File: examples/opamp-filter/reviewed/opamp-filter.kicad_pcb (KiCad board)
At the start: 2 copper layers, 58 x 42 mm, 22 parts, among them J1 IN, J2 5V, J3 OUT, U1 MCP6001R, U2 MCP6001R

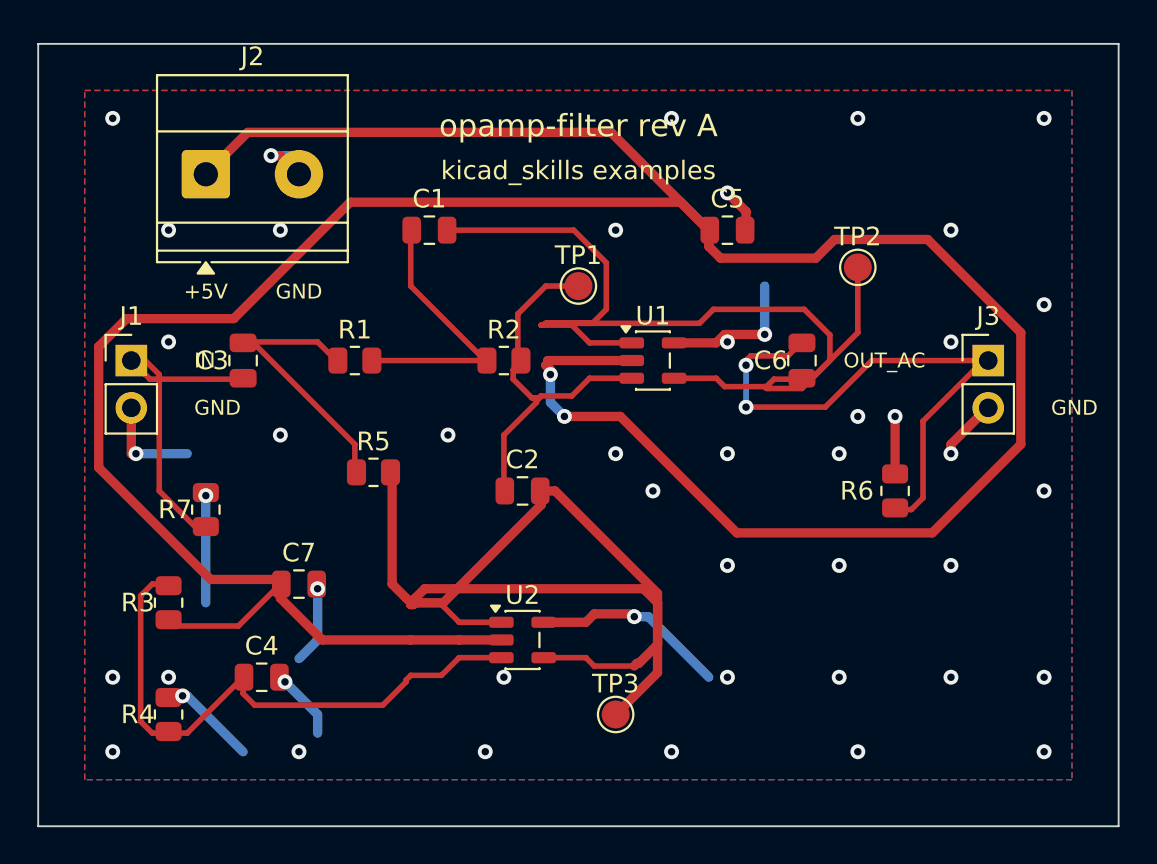
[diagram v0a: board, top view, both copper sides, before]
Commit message: Measure the copper that goes out and comes back, and the text drawn on text
The reviewer sent screenshots with circles on them. Two kinds: strings
printed through each other on the schematics, and copper that leaves a
pad, travels three sides of a rectangle and arrives four millimetres
away. Neither had a rule that could see it - `text_over_wire` measured
text against nets and nothing measured text against text, and
`route.detour` weighs a whole net, which averages one bad connection
away under any ratio worth setting.

New rule `route.wander`: one continuous run of copper - pad or junction
at each end - against the shortest way between those two ends that
clears the packages in between. The baseline walks the perimeter of
whatever the straight line crosses, so an opamp's feedback wrap is
measured against going round the package rather than through it. On
KiCad's 18 demo boards it fires once at the shipped 2.0x.

`readability.text_over_text` and `_over_wire` are regraded info: they
fire on 14 and 10 of those 18 human sheets. That is the estimate
talking, not the drawing. `ai-generated` still promotes both to errors,
so every generated design has to have none - and the five examples do.

What the two rules then made us fix:

* a net label's anchor cannot move, but its reading direction can. Each
  name is now offered the four quarters of its anchor and takes the
  first that prints over nothing. Power symbol names and PWR_FLAG names
  get the same treatment - four grounds on one row printed GNGNGNGND.
  Schematic text overlaps: buck 1, motor 2, carrier 1, fpga 7, all to 0.
* a plane crossing was priced at forty times front copper per
  millimetre, which is a prohibition, not a price: one millimetre of
  crossing bought a forty millimetre tour and the boards had grown
  them. Thirty is where neither `route.wander` nor `route.return_path`
  fires. Buck, motor and carrier now have no wander findings.
* `write_variant` resolves the routes a second time, so the
  straight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
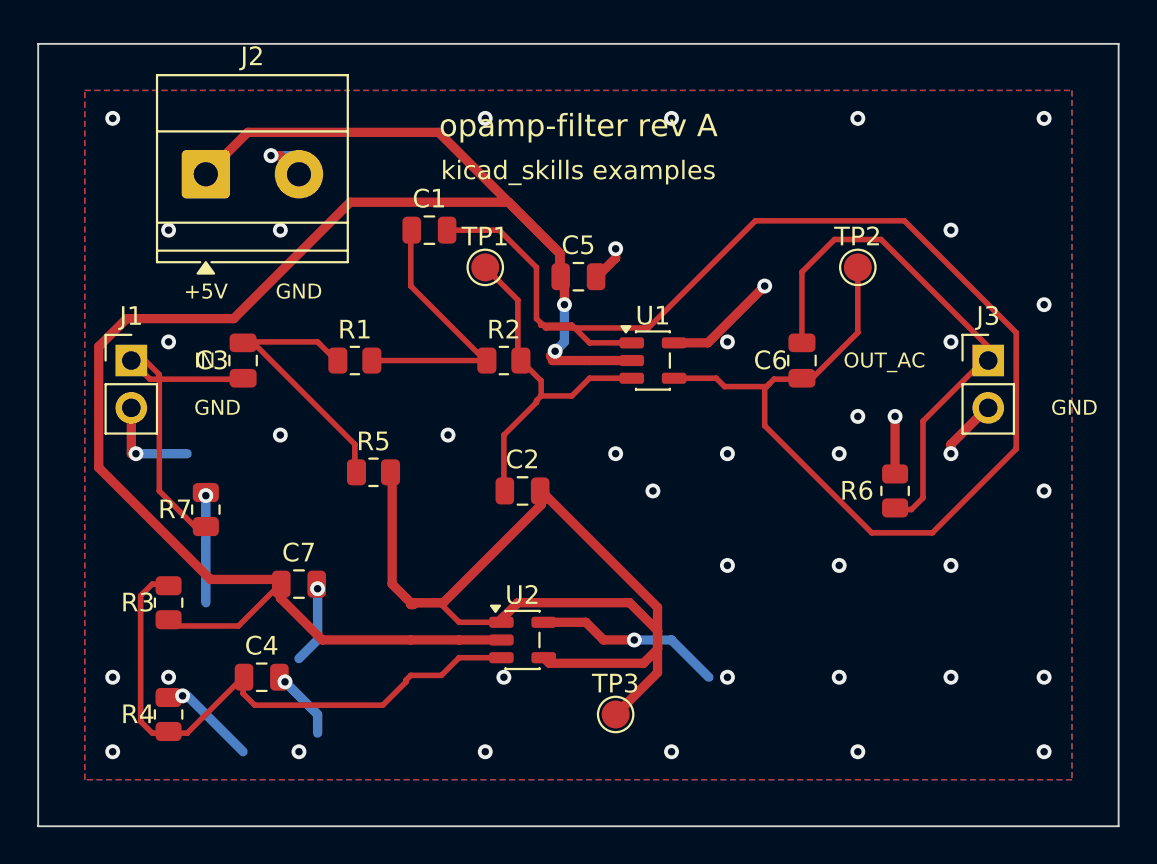
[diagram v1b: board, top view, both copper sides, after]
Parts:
- moved C5 8.38 mm to (129.0, 72.5)
- moved TP1 5.10 mm to (124.0, 72.0)
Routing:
- net +5V: track 169.8 -> 103.1 mm
- net /OUT: track 57.6 -> 85.4 mm
- net /VREF: track 61.8 -> 55.5 mm
- net GND: track 55.4 -> 53.0 mm
- net /OUT_AC: track 30.7 -> 28.4 mm, vias 2 -> 0
- net /FILT_IN: track 20.8 -> 19.3 mm

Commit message: Stop hiding the hairpins behind the pads they are drawn on
The reviewer said the 135 degree bends and the odd-angle runs were still
there. They were. `route.acute_angle` skipped any corner within a pad's
*radius*, and a 0805's radius is 0.47 mm, which covers the five or six
ordinary corners a chamfered pad entry leaves inside it. Eleven of the
thirteen hairpins on these five boards sat in that shadow, because a pad
is exactly where a route that has to double back does it.

The exemption is the pad's connection point now, not a disc around it.
Two branches leaving one pad stay exempt - the pad's own copper fills the
wedge, so it is not an acid trap - but nought degrees never is: that is
one run drawn twice, and no pad excuses it.

Then the generator had to stop making them:

* `_untraced` drops the copper a second run lays on top of the first.
  The shorter is inside the longer and carries nothing it does not; both
  get trimmed, because dropping only the duplicate leaves the other
  hanging over the gap, which is `route.stub`. It runs before the runs
  are joined, while the pair is still two tracks sharing an end - once
  joined, the shared point is usually a pad, and the clean-up passes pin
  those precisely so they cannot take copper off them.
* `_straighten` only takes the direct line when it lands on the 45 grid.
  Between two pads at whatever coordinates their packages give them it
  usually does not: last round it made a nine millimetre run at 169.7
  degrees, which is the slip-of-the-mouse angle `route.odd_angle` is for.

Measured across the five boards: off-grid segments 1 to 0, 180 degree
reversals 6 to 0, and the motor board's `route.return_path` finding went
with the 11 mm of copper it was measuring.

Three corners survive, all on the FPGA board, all where a knee lands a
fraction past where its own two legs cross - legs of 0.07 and 0.25 mm on
two, 0.15 and 0.5 mm on the third. Refusing a knee that short is worse:
the segment then keeps the angle it had, a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
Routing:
- net GND: track 53.0 -> 53.8 mm
- net /FILT_IN: track 19.3 -> 20.1 mm
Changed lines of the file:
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@@
 	(segment (start 129.6 77.95) (end 128.65 78.9) (width 0.3) (layer "F.Cu") (net 3))
 	(segment (start 128.65 78.9) (end 127.0 78.9) (width 0.3) (layer "F.Cu") (net 3))
-	(segment (start 134.1375 76.05) (end 135.95 76.05) (width 0.5) (layer "F.Cu") (net 1))
-	(segment (start 135.95 76.05) (end 139.0 73.0) (width 0.5) (layer "F.Cu") (net 1))
+	(segment (start 134.1375 76.05) (end 136.4 76.05) (width 0.5) (layer "F.Cu") (net 1))
+	(segment (start 136.4 76.05) (end 136.85 75.6) (width 0.5) (layer "F.Cu") (net 1))
+	(segment (start 136.85 75.6) (end 137.925 75.6) (width 0.5) (layer "F.Cu") (net 1))
+	(segment (start 137.925 75.6) (end 139.0 74.525) (width 0.5) (layer "F.Cu") (net 1))
+	(segment (start 139.0 74.525) (end 139.0 73.0) (width 0.5) (layer "F.Cu") (net 1))
 	(segment (start 134.1375 77.95) (end 136.4 77.95) (width 0.3) (layer "F.Cu") (net 7))
 	(segment (start 136.4 77.95) (end 136.85 78.4) (width 0.3) (layer "F.Cu") (net 7))
@@
 	(segment (start 111.0 94.875) (end 111.0 94.25) (width 0.3) (layer "F.Cu") (net 6))
 	(segment (start 111.0 94.25) (end 111.05 94.2) (width 0.3) (layer "F.Cu") (net 6))
-	(segment (start 111.05 94.2) (end 111.05 94.0) (width 0.3) (layer "F.Cu") (net 6))
-	(segment (start 111.05 94.0) (end 110.8 94.25) (width 0.3) (layer "F.Cu") (net 6))
+	(segment (start 111.05 94.2) (end 110.95 94.1) (width 0.3) (layer "F.Cu") (net 6))
+	(segment (start 110.95 94.1) (end 110.8 94.25) (width 0.3) (layer "F.Cu") (net 6))
 	(segment (start 110.8 94.25) (end 110.75 94.25) (width 0.3) (layer "F.Cu") (net 6))
 	(segment (start 110.75 94.25) (end 108.0 97.0) (width 0.3) (layer "F.Cu") (net 6))
@@
 	(segment (start 108.75 86.0) (end 108.9125 86.0) (width 0.3) (layer "F.Cu") (net 4))
 	(segment (start 108.9125 86.0) (end 109.0 85.9125) (width 0.3) (layer "F.Cu") (net 4))
-	(segment (start 116.0875 77.0) (end 115.8375 76.75) (width 0.3) (layer "F.Cu") (net 5))
-	(segment (start 115.8375 76.75) (end 115.75 76.75) (width 0.3) (layer "F.Cu") (net 5))
-	(segment (start 115.75 76.75) (end 115.0 76.0) (width 0.3) (layer "F.Cu") (net 5))
-	(segment (start 115.0 76.0) (end 111.25 76.0) (width 0.3) (layer "F.Cu") (net 5))
-	(segment (start 111.25 76.0) (end 111.2 76.05) (width 0.3) (layer "F.Cu") (net 5))
-	(segment (start 111.2 76.05) (end 111.0 76.05) (width 0.3) (layer "F.Cu") (net 5))
+	(segment (start 111.2 76.05) (end 111.25 76.0) (width 0.3) (layer "F.Cu") (net 5))
+	(segment (start 111.25 76.0) (end 115.0 76.0) (width 0.3) (layer "F.Cu") (net 5))
+	(segment (start 115.0 76.0) (end 115.75 76.75) (width 0.3) (layer "F.Cu") (net 5))
+	(segment (start 115.75 76.75) (end 115.8375 76.75) (width 0.3) (layer "F.Cu") (net 5))
+	(segment (start 115.8375 76.75) (end 116.0875 77.0) (width 0.3) (layer "F.Cu") (net 5))
 	(segment (start 111.0 76.05) (end 111.2 76.05) (width 0.3) (layer "F.Cu") (net 5))
 	(segment (start 111.2 76.05) (end 111.25 76.0) (width 0.3) (layer "F.Cu") (net 5))
@@
 	(segment (start 117.0 82.9125) (end 117.0875 83.0) (width 0.3) (layer "F.Cu") (net 5))
 	(segment (start 117.9125 77.0) (end 124.0875 77.0) (width 0.3) (layer "F.Cu") (net 10))
-	(segment (start 124.0875 77.0) (end 124.0 77.0) (width 0.3) (layer "F.Cu") (net 10))
 	(segment (start 124.0 77.0) (end 123.75 76.75) (width 0.3) (layer "F.Cu") (net 10))
 	(segment (start 123.75 76.75) (end 120.0 73.0) (width 0.3) (layer "F.Cu") (net 10))
@@
 	(segment (start 120.0 70.25) (end 120.0 70.05) (width 0.3) (layer "F.Cu") (net 10))
 	(segment (start 120.0 70.05) (end 120.05 70.0) (width 0.3) (layer "F.Cu") (net 10))
-	(segment (start 127.0 78.9) (end 127.0 78.0875) (width 0.3) (layer "F.Cu") (net 3))
-	(segment (start 127.0 78.0875) (end 125.9125 77.0) (width 0.3) (layer "F.Cu") (net 3))
+	(segment (start 127.0 78.9) (end 126.9 79.0) (width 0.3) (layer "F.Cu") (net 3))
+	(segment (start 126.9 79.0) (end 126.75 79.0) (width 0.3) (layer "F.Cu") (net 3))
+	(segment (start 126.75 79.0) (end 126.5 79.0) (width 0.3) (layer "F.Cu") (net 3))
+	(segment (start 126.5 79.0) (end 125.5 78.0) (width 0.3) (layer "F.Cu") (net 3))
+	(segment (start 125.5 78.0) (end 125.5 77.5) (width 0.3) (layer "F.Cu") (net 3))
+	(segment (start 125.5 77.5) (end 125.75 77.25) (width 0.3) (layer "F.Cu") (net 3))
+	(segment (start 125.75 77.25) (end 125.9125 77.0875) (width 0.3) (layer "F.Cu") (net 3))
+	(segment (start 125.9125 77.0875) (end 125.9125 77.0) (width 0.3) (layer "F.Cu") (net 3))
 	(segment (start 125.9125 77.0) (end 125.75 76.8375) (width 0.3) (layer "F.Cu") (net 3))
 	(segment (start 125.75 76.8375) (end 125.75 76.75) (width 0.3) (layer "F.Cu") (net 3))
@@
 	(segment (start 127.25 84.25) (end 127.2 84.25) (width 0.5) (layer "F.Cu") (net 9))
 	(segment (start 127.2 84.25) (end 126.95 84.0) (width 0.5) (layer "F.Cu") (net 9))
-	(segment (start 126.95 84.0) (end 127.0 84.05) (width 0.5) (layer "F.Cu") (net 9))
-	(segment (start 127.0 84.05) (end 127.0 84.25) (width 0.5) (layer "F.Cu") (net 9))
-	(segment (start 127.0 84.25) (end 127.0 84.75) (width 0.5) (layer "F.Cu") (net 9))
-	(segment (start 127.0 84.75) (end 121.75 90.0) (width 0.5) (layer "F.Cu") (net 9))
-	(segment (start 121.75 90.0) (end 120.25 90.0) (width 0.5) (layer "F.Cu") (net 9))
-	(segment (start 120.25 90.0) (end 120.15 90.1) (width 0.5) (layer "F.Cu") (net 9))
-	(segment (start 120.15 90.1) (end 120.0 90.1) (width 0.5) (layer "F.Cu") (net 9))
 	(segment (start 125.05 84.0) (end 125.05 83.8) (width 0.3) (layer "F.Cu") (net 3))
 	(segment (start 125.05 83.8) (end 125.0 83.75) (width 0.3) (layer "F.Cu") (net 3))
@@
 	(segment (start 127.5 93.25) (end 127.4375 93.25) (width 0.5) (layer "F.Cu") (net 9))
 	(segment (start 127.4375 93.25) (end 127.1375 92.95) (width 0.5) (layer "F.Cu") (net 9))
+	(segment (start 120.0 90.1) (end 120.15 90.1) (width 0.5) (layer "F.Cu") (net 9))
+	(segment (start 120.15 90.1) (end 120.25 90.0) (width 0.5) (layer "F.Cu") (net 9))
+	(segment (start 120.25 90.0) (end 121.75 90.0) (width 0.5) (layer "F.Cu") (net 9))
+	(segment (start 121.75 90.0) (end 127.0 84.75) (width 0.5) (layer "F.Cu") (net 9))
+	(segment (start 127.0 84.75) (end 127.0 84.25) (width 0.5) (layer "F.Cu") (net 9))
+	(segment (start 127.0 84.25) (end 127.0 84.05) (width 0.5) (layer "F.Cu") (net 9))
 	(segment (start 120.0 90.1) (end 120.0 90.0) (width 0.5) (layer "F.Cu") (net 9))
 	(segment (start 120.0 90.0) (end 119.75 89.75) (width 0.5) (layer "F.Cu") (net 9))
